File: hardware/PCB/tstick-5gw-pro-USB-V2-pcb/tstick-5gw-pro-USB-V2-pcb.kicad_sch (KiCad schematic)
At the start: 51 parts, among them J1 USB_C_Receptacle_USB2.0, J2 GPIO2, J3 GPIO1, Q3 BSS138, SW1 JST-SH-1.00mm 1x2, SW2 PTS810 SJM Switch, SW3 PTS810 SJM Switch, U1 max8819ceti+, U4 PCA9306DP

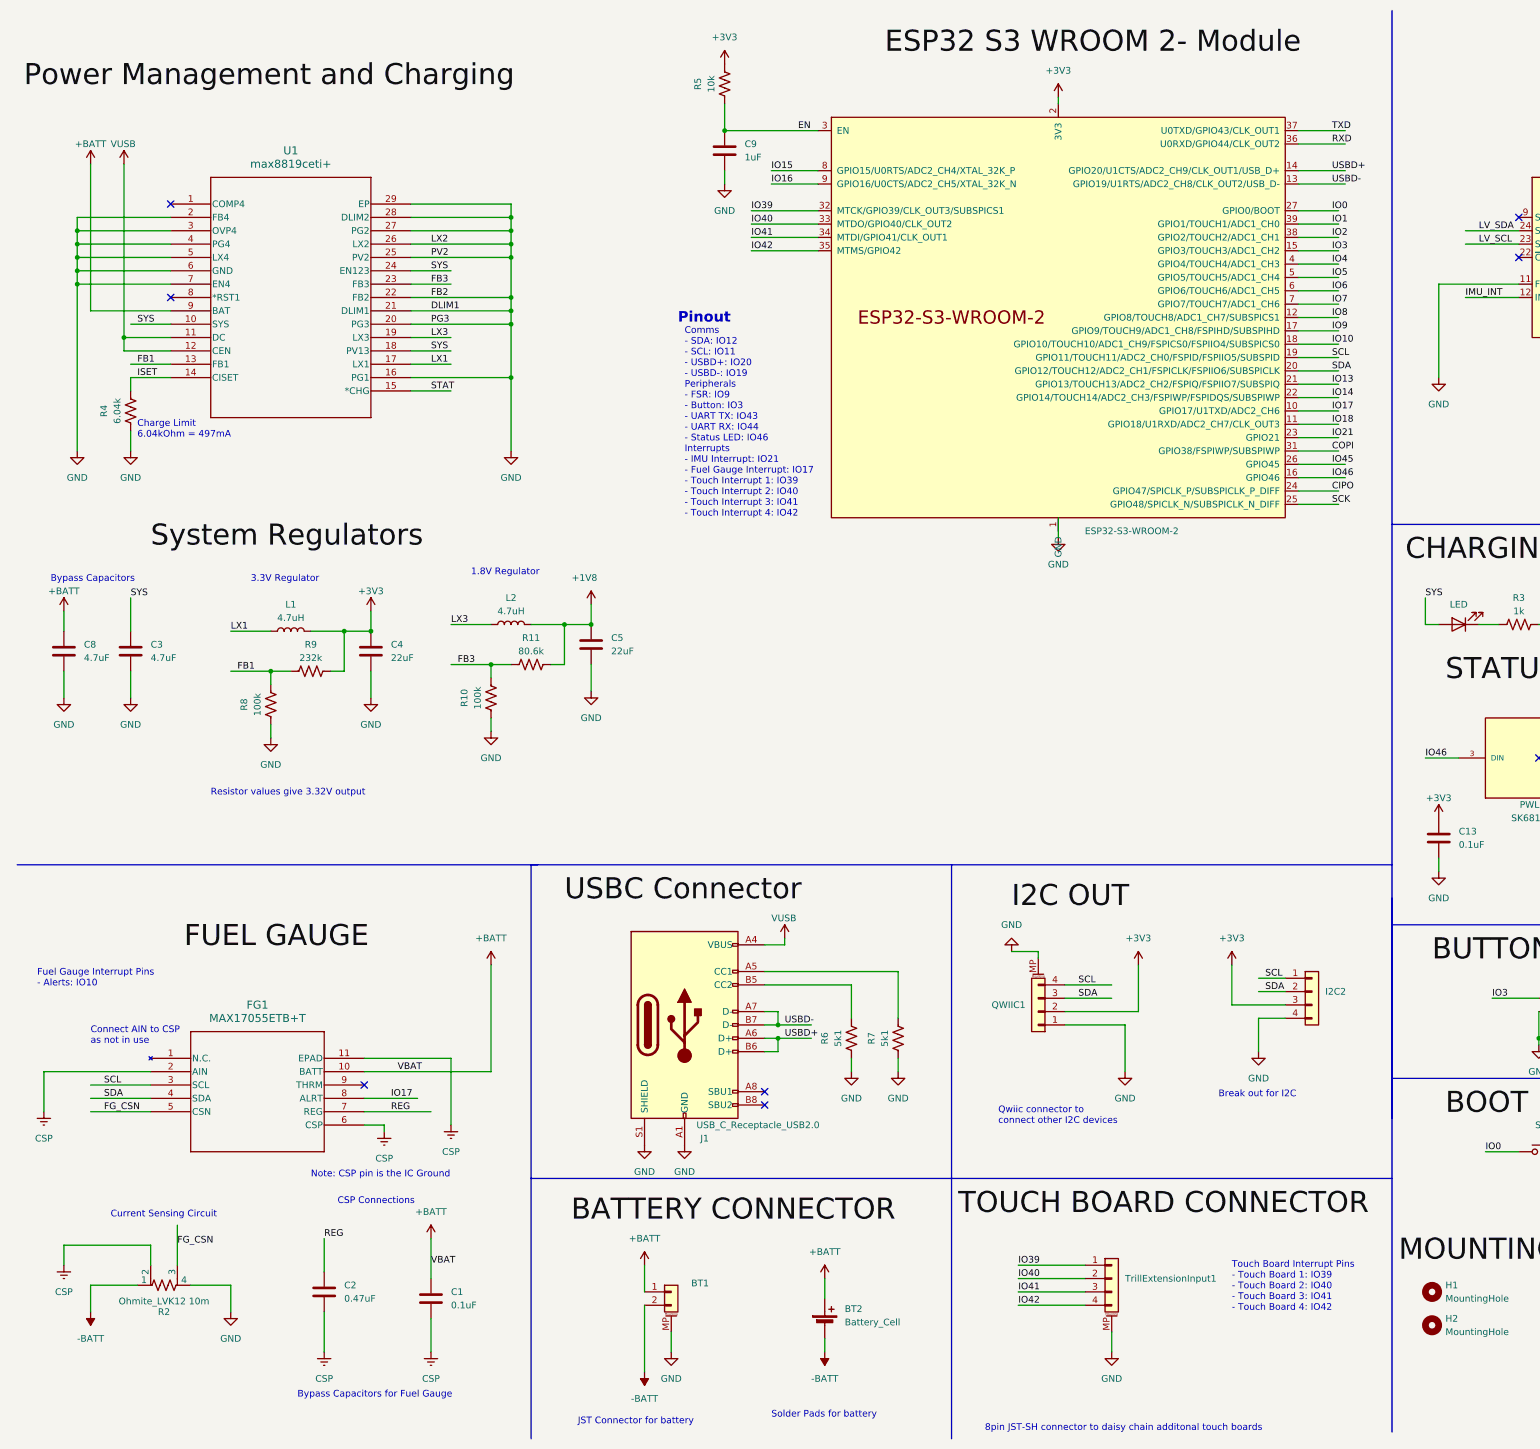
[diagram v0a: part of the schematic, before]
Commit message: added thermistor
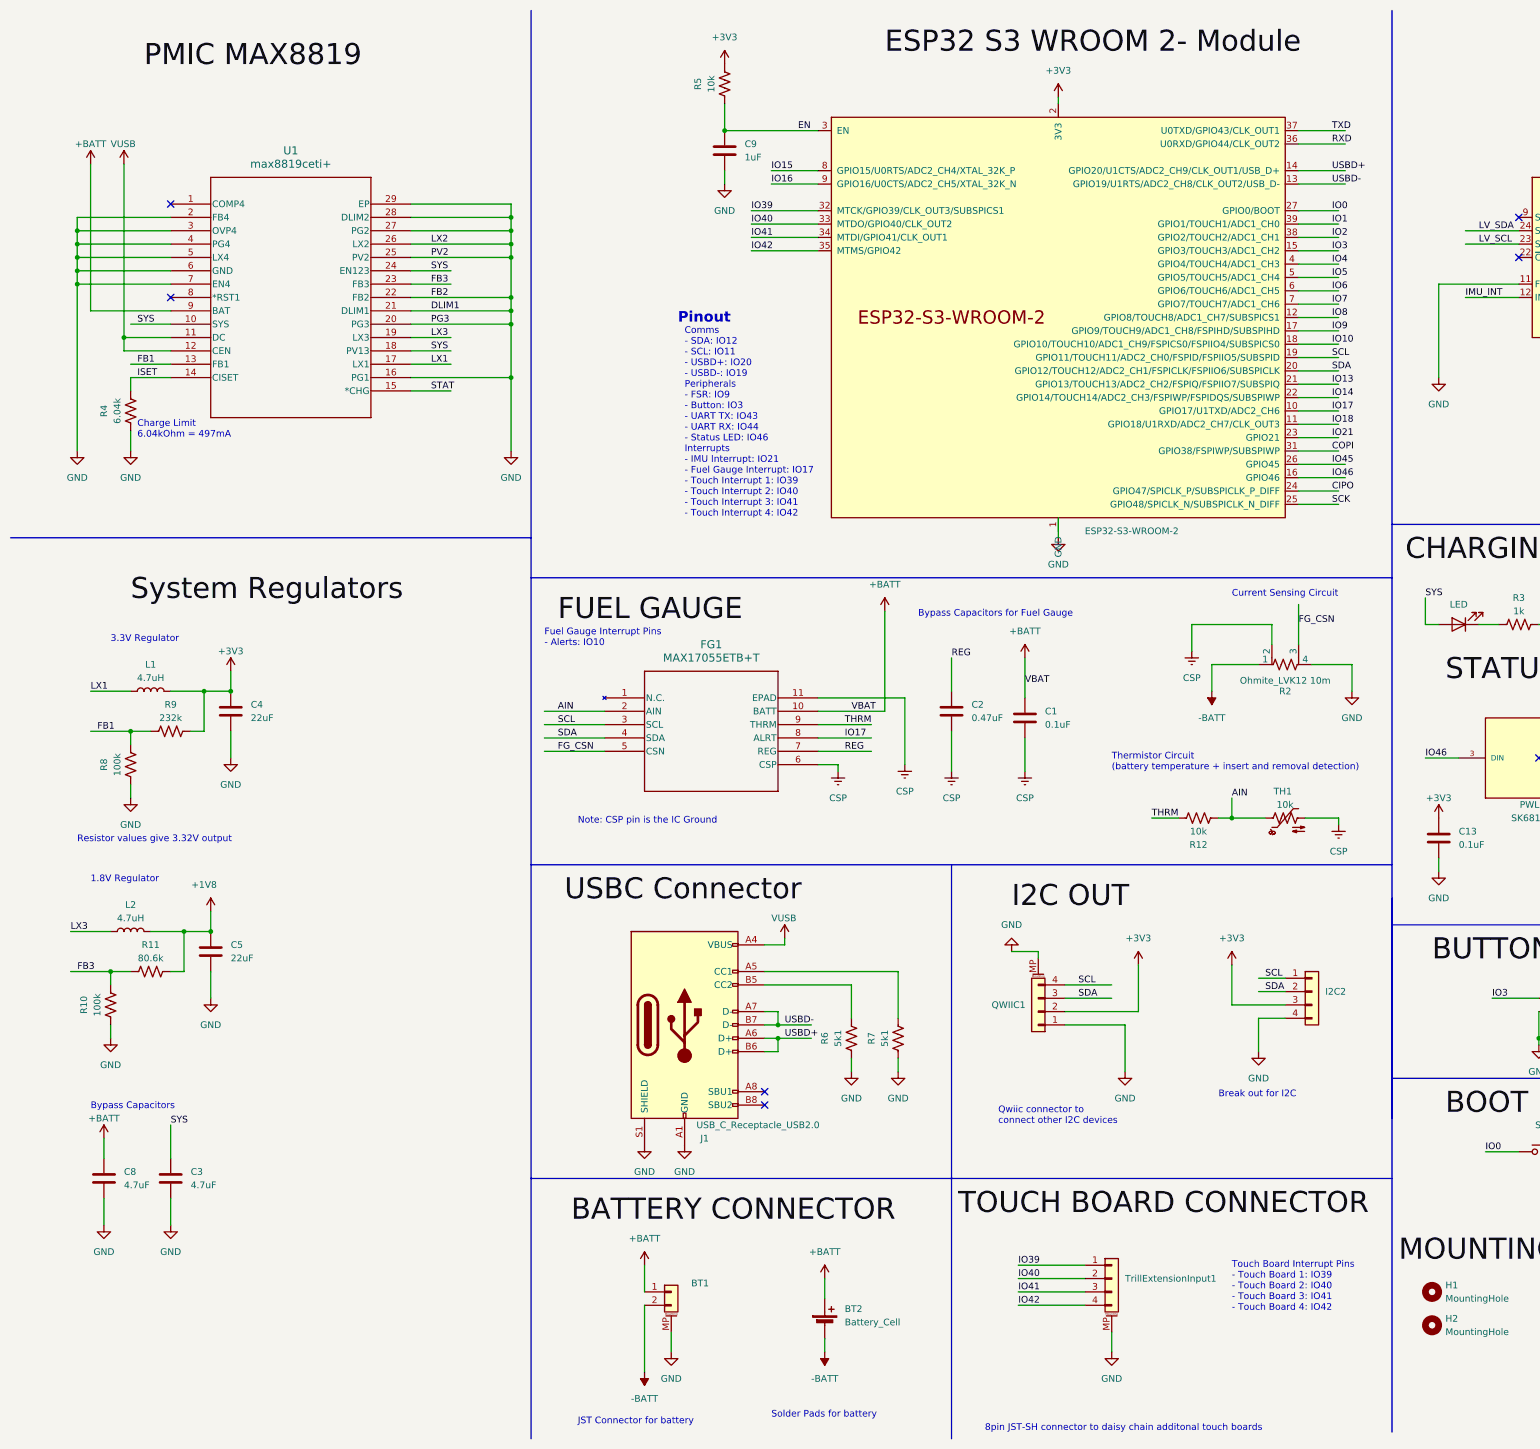
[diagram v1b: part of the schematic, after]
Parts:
- added R12: 10k, Resistor_SMD:R_0201_0603Metric, symbol Device:R_US
- added TH1: 10k, Resistor_SMD:R_0201_0603Metric, symbol Device:Thermistor_NTC_US
- J2, J3: now left out of the parts list
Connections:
- net CSP: now also TH1.2; no longer FG1.2 (AIN)
- net THRM: now reaches FG1.9 (THRM)
- net THRM: now also R12.2
- new net AIN: FG1.2 (AIN), R12.1, TH1.1
- no-connect marks 12 -> 11
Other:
- note added: "Thermistor Circuit (battery temperature + insert and removal detection)"
- note removed: "CSP Connections"
- note removed: "Connect AIN to CSP as not in use"
- moved on the sheet: C1, C2, C3, C4, C5, C8, FG1, L1, L2, R10, R11, R2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

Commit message: cleaned up v1 of the boards, fixed issue with evt2 trace not being connected in touch board
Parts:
- added SYS1, SYS2: SYS, symbol power-symbols:VSYS
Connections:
- net -BATT: now also TH1.2
- net CSP: no longer TH1.2
- net SYS: now also SYS1.1 (SYS), SYS2.1 (SYS)
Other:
- note added: "SYS is the System Voltage, set to 4.35V by main regulator"
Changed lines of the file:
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@@
   (junction (at 358.14 34.29) (diameter 0) (color 0 0 0 0)
   )
+  (junction (at 97.79 62.23) (diameter 0) (color 0 0 0 0)
+  )
   (junction (at 106.68 52.07) (diameter 0) (color 0 0 0 0)
   )
@@
     (stroke (width 0) (type default))
   )
+  (wire (pts (xy 87.63 77.47) (xy 97.79 77.47))
+    (stroke (width 0) (type default))
+  )
   (wire (pts (xy 256.54 78.74) (xy 264.16 78.74))
     (stroke (width 0) (type default))
@@
     (stroke (width 0) (type default))
   )
-  (wire (pts (xy 87.63 62.23) (xy 95.25 62.23))
+  (wire (pts (xy 87.63 62.23) (xy 97.79 62.23))
     (stroke (width 0) (type default))
   )
@@
     (stroke (width 0) (type default))
   )
+  (wire (pts (xy 97.79 41.91) (xy 97.79 62.23))
+    (stroke (width 0) (type default))
+  )
   (wire (pts (xy 24.13 57.15) (xy 41.91 57.15))
     (stroke (width 0) (type default))
@@
     (stroke (width 0) (type default))
   )
+  (wire (pts (xy 38.1 72.39) (xy 41.91 72.39))
+    (stroke (width 0) (type default))
+  )
   (wire (pts (xy 24.13 54.61) (xy 41.91 54.61))
     (stroke (width 0) (type default))
@@
     (stroke (width 0) (type default))
   )
-  (wire (pts (xy 34.29 72.39) (xy 41.91 72.39))
-    (stroke (width 0) (type default))
-  )
   (wire (pts (xy 203.2 256.54) (xy 215.9 256.54))
     (stroke (width 0) (type default))
@@
     (stroke (width 0) (type default))
   )
+  (wire (pts (xy 38.1 41.91) (xy 38.1 72.39))
+    (stroke (width 0) (type default))
+  )
   (wire (pts (xy 360.68 78.74) (xy 360.68 82.55))
     (stroke (width 0) (type default))
@@
     (stroke (width 0) (type default))
   )
+  (wire (pts (xy 97.79 62.23) (xy 97.79 77.47))
+    (stroke (width 0) (type default))
+  )
   (wire (pts (xy 41.91 224.79) (xy 41.91 231.14))
     (stroke (width 0) (type default))
@@
     (stroke (width 0) (type default))
   )
-  (wire (pts (xy 87.63 77.47) (xy 95.25 77.47))
-    (stroke (width 0) (type default))
-  )
   (wire (pts (xy 302.26 208.28) (xy 307.34 208.28))
     (stroke (width 0) (type default))
@@
     (effects (font (size 1.27 1.27)) (justify left bottom))
   )
+  (text "SYS is the System Voltage, set to 4.35V \nby main regulator\n\n\n\n"
+    (at 69.85 43.18 0)
+    (effects (font (size 1.27 1.27)) (justify left bottom))
+  )
   (label "IMU_INT" (at 351.79 96.52 0) (fields_autoplaced)
     (effects (font (size 1.27 1.27)) (justify left bottom))
@@
     (effects (font (size 1.27 1.27)) (justify left bottom))
   )
-  (label "SYS" (at 91.44 77.47 0) (fields_autoplaced)
-    (effects (font (size 1.27 1.27)) (justify left bottom))
-  )
   (label "USBD+" (at 262.89 43.18 0) (fields_autoplaced)
     (effects (font (size 1.27 1.27)) (justify left bottom))
@@
     (effects (font (size 4 4)) (justify left bottom))
   )
-  (label "SYS" (at 35.56 72.39 0) (fields_autoplaced)
-    (effects (font (size 1.27 1.27)) (justify left bottom))
-  )
   (label "IO8" (at 378.46 142.24 0) (fields_autoplaced)
     (effects (font (size 1.27 1.27)) (justify left bottom))
@@
     )
   )
+  (symbol (lib_id "power:-BATT") (at 264.16 167.64 180) (unit 1)
+    (in_bom yes) (on_board yes) (dnp no)
+    (property "Reference" "#PWR032" (at 264.16 163.83 0)
+      (effects (font (size 1.27 1.27)) hide)
+    )
+    (property "Value" "-BATT" (at 264.16 172.72 0)
+      (effects (font (size 1.27 1.27)))
+    )
+    (property "Footprint" "" (at 264.16 167.64 0)
+      (effects (font (size 1.27 1.27)) hide)
+    )
+    (property "Datasheet" "" (at 264.16 167.64 0)
+      (effects (font (size 1.27 1.27)) hide)
+    )
+    (pin "1")
+    (instances
+      (project "tstick-5gw-pro-USB-V2-pcb"
+        (path "/1e57a4ff-0c95-4e2b-9e56-d9bf8e99c9a1"
+          (reference "#PWR032") (unit 1)
+        )
+      )
+      (project "tstick_pcb"
+        (path "/ecdbf224-0069-4dc3-a7df-492909ab59c7"
+          (reference "#PWR034") (unit 1)
+        )
+      )
+    )
+  )
   (symbol (lib_id "Device:R_US") (at 358.14 40.64 180) (unit 1)
     (in_bom yes) (on_board yes) (dnp no)
@@
     )
   )
+  (symbol (lib_id "power-symbols:VSYS") (at 38.1 41.91 0) (unit 1)
+    (in_bom yes) (on_board yes) (dnp no)
+    (property "Reference" "SYS1" (at 38.1 35.56 0)
+      (effects (font (size 1.27 1.27)) hide)
+    )
+    (property "Value" "SYS" (at 36.83 38.1 0)
+      (effects (font (size 1.27 1.27)) (justify left))
+    )
+    (property "Footprint" "" (at 38.1 41.91 0)
+      (effects (font (size 1.27 1.27)) hide)
+    )
+    (property "Datasheet" "" (at 38.1 41.91 0)
+      (effects (font (size 1.27 1.27)) hide)
+    )
+    (pin "1")
+    (instances
+      (project "tstick-5gw-pro-USB-V2-pcb"
+        (path "/1e57a4ff-0c95-4e2b-9e56-d9bf8e99c9a1"
+          (reference "SYS1") (unit 1)
+        )
+      )
+    )
+  )
   (symbol (lib_id "Switch:SW_Push") (at 373.38 231.14 0) (unit 1)
     (in_bom yes) (on_board yes) (dnp no) (fields_autoplaced)
@@
     )
   )
-  (symbol (lib_id "max17055-symbol:CSP") (at 264.16 168.91 0) (unit 1)
-    (in_bom yes) (on_board yes) (dnp no) (fields_autoplaced)
-    (property "Reference" "#ICGND05" (at 264.16 175.26 0)
-      (effects (font (size 1.27 1.27)) hide)
-    )
-    (property "Value" "CSP" (at 264.16 172.72 0)
-      (effects (font (size 1.27 1.27)))
-    )
-    (property "Footprint" "" (at 260.35 168.91 0)
-      (effects (font (size 1.27 1.27)) hide)
-    )
-    (property "Datasheet" "" (at 260.35 168.91 0)
-      (effects (font (size 1.27 1.27)) hide)
-    )
-    (pin "1")
-    (instances
-      (project "tstick-5gw-pro-USB-V2-pcb"
-        (path "/1e57a4ff-0c95-4e2b-9e56-d9bf8e99c9a1"
-          (reference "#ICGND05") (unit 1)
-        )
-      )
-      (project "tstick_pcb"
-        (path "/ecdbf224-0069-4dc3-a7df-492909ab59c7"
-          (reference "#ICGND04") (unit 1)
-        )
-      )
-    )
-  )
   (symbol (lib_name "GND_2") (lib_id "power:GND") (at 345.44 157.48 0) (unit 1)
     (in_bom yes) (on_board yes) (dnp no) (fields_autoplaced)
@@
         )
       )
+    )
+  )
+  (symbol (lib_id "power-symbols:VSYS") (at 97.79 41.91 0) (unit 1)
+    (in_bom yes) (on_board yes) (dnp no)
+    (property "Reference" "SYS2" (at 97.79 35.56 0)
+      (effects (font (size 1.27 1.27)) hide)
+    )
+    (property "Value" "SYS" (at 96.52 38.1 0)
+      (effects (font (size 1.27 1.27)) (justify left))
+    )
+    (property "Footprint" "" (at 97.79 41.91 0)
+      (effects (font (size 1.27 1.27)) hide)
+    )
+    (property "Datasheet" "" (at 97.79 41.91 0)
+      (effects (font (size 1.27 1.27)) hide)
+    )
+    (pin "1")
+    (instances
+      (project "tstick-5gw-pro-USB-V2-pcb"
+        (path "/1e57a4ff-0c95-4e2b-9e56-d9bf8e99c9a1"
+          (reference "SYS2") (unit 1)
+        )
+      )
